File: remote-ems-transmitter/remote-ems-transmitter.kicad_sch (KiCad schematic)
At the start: 50 parts, among them IC1 Wio-E5, J1 Conn_01x04_Pin, J2 Conn_01x02, J3 Conn_01x02, J4 Conn_Coaxial, J5 USB_C_Receptacle_USB2.0, Q1 BSS138, SW1 SW_Push, SW2 SW_Push, SW3 SW_Push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

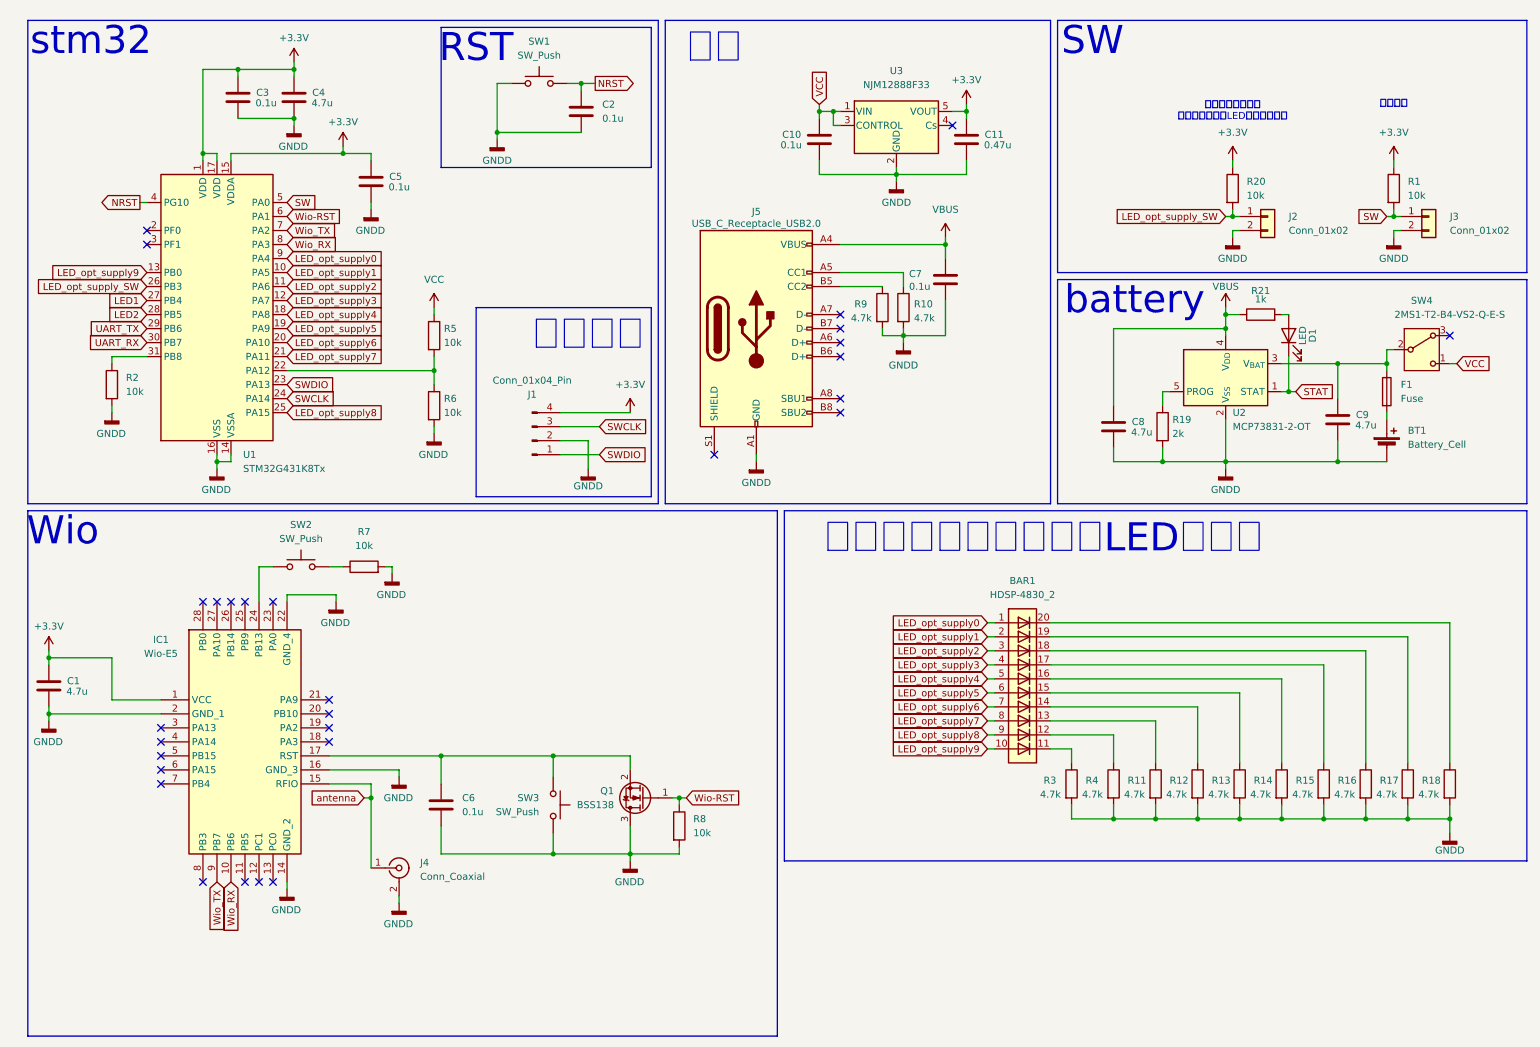
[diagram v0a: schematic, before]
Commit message: remote-ems-transmitter　ビア、シルク、LED以外完成
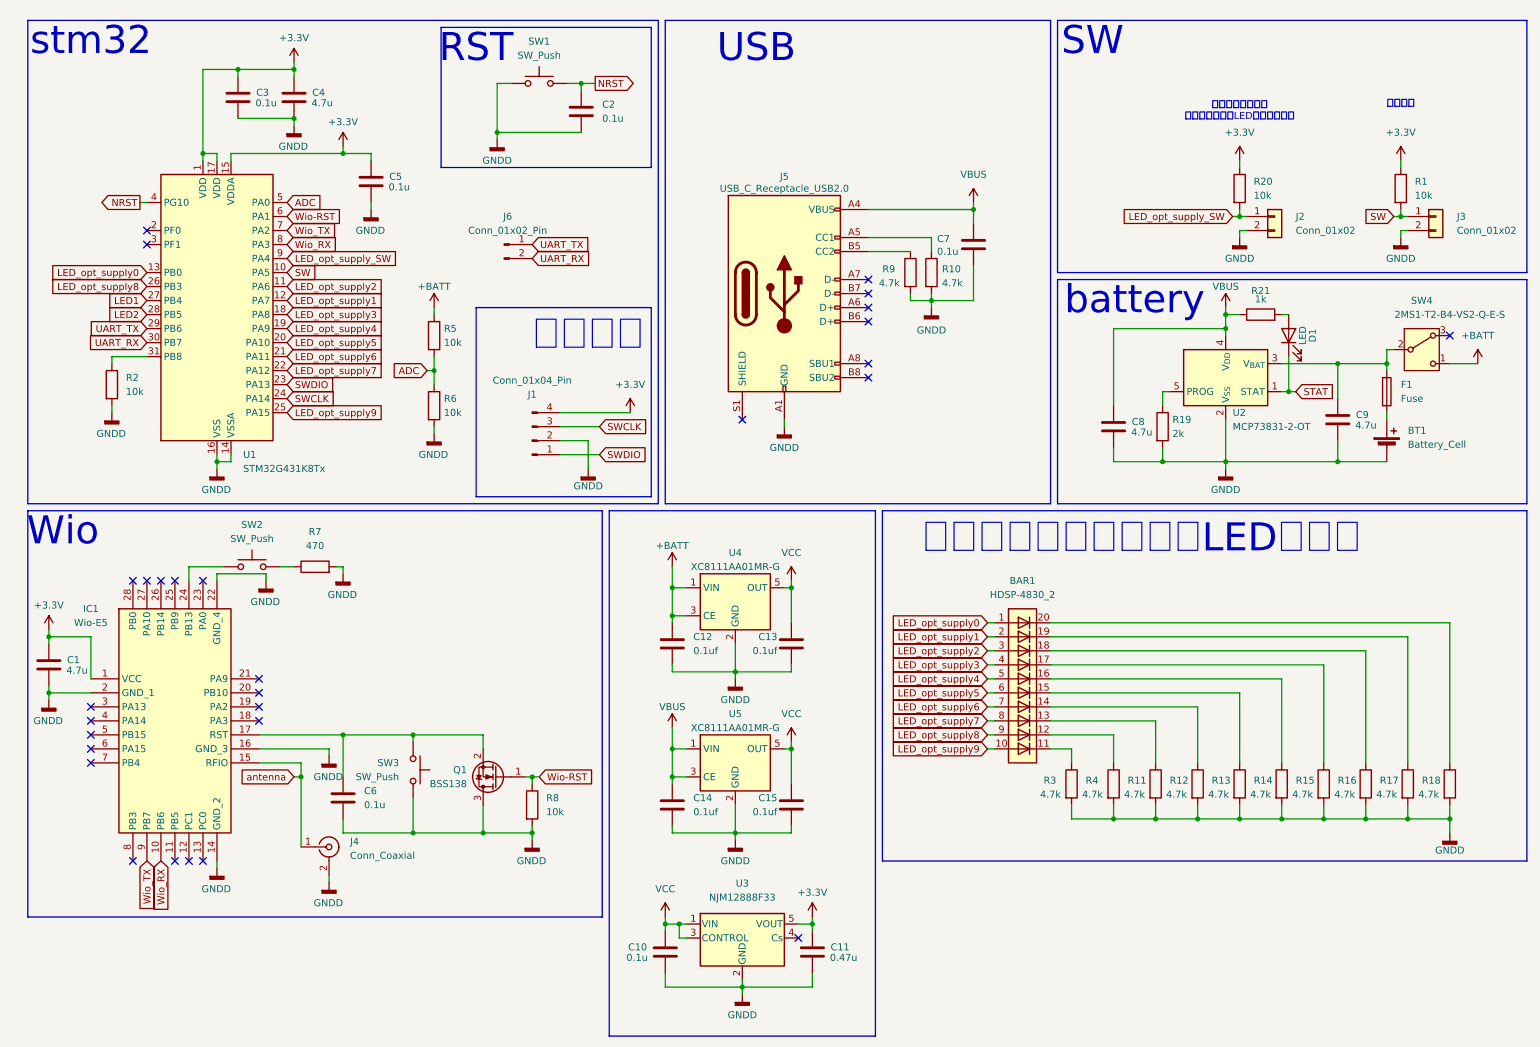
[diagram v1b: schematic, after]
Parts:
- added C12, C13, C14, C15: 0.1uf, Capacitor_SMD:C_0603_1608Metric_Pad1.08x0.95mm_HandSolder, symbol Device:C
- added J6: Conn_01x02_Pin, Connector_PinHeader_2.54mm:PinHeader_1x02_P2.54mm_Vertical, symbol Connector:Conn_01x02_Pin
- added U4, U5: XC8111AA01MR-G, Package_TO_SOT_SMD:SOT-23-5_HandSoldering, symbol Analog_Switch:MAX40200AUK
- BT1: footprint Connector_JST:JST_XH_B2B-XH-A_1x02_P2.50mm_Vertical -> Connector_JST:JST_PH_B2B-PH-K_1x02_P2.00mm_Vertical
- R7: value 10k -> 470
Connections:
- net GNDD: now also C12.2, C13.2, C14.2, C15.2, U4.2 (GND), U5.2 (GND)
- net LED_opt_supply0: now also U1.13 (PB0); no longer U1.9 (PA4)
- net LED_opt_supply1: now also U1.12 (PA7); no longer U1.10 (PA5)
- net LED_opt_supply3: now also U1.18 (PA8); no longer U1.12 (PA7)
- net LED_opt_supply4: now also U1.19 (PA9); no longer U1.18 (PA8)
- net LED_opt_supply5: now also U1.20 (PA10); no longer U1.19 (PA9)
- net LED_opt_supply6: now also U1.21 (PA11); no longer U1.20 (PA10)
- net LED_opt_supply7: now also U1.22 (PA12); no longer U1.21 (PA11)
- net LED_opt_supply8: now also U1.26 (PB3); no longer U1.25 (PA15)
- net LED_opt_supply9: now also U1.25 (PA15); no longer U1.13 (PB0)
- net LED_opt_supply_SW: now also U1.9 (PA4); no longer U1.26 (PB3)
- net SW: now also U1.10 (PA5); no longer U1.5 (PA0)
- net UART_RX: now also J6.2 (Pin_2)
- net UART_TX: now also J6.1 (Pin_1)
- net VBUS: now also C14.1, U5.1 (VIN), U5.3 (CE)
- net VCC: now also C13.1, C15.1, U4.5 (OUT), U5.5 (OUT); no longer R5.1, SW4.1 (C)
- net ADC: now reaches R5.2, R6.1
- net ADC: now also U1.5 (PA0); no longer U1.22 (PA12)
- new net +BATT: C12.1, R5.1, SW4.1 (C), U4.1 (VIN), U4.3 (CE)
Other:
- note added: "USB"
- note removed: "電源"
- moved on the sheet: C1, C10, C11, C6, C7, IC1, J2, J3, J4, J5, Q1, R1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

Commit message: LED周り修正
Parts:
- removed R21: 1k, Resistor_SMD:R_0603_1608Metric_Pad0.98x0.95mm_HandSolder, symbol Device:R
- added BAR2: OSX40601-AO, 0Ikedalibrary:OSX40601-AO, symbol LED:HDSP-4830_2
- added D2: LED, LED_THT:LED_D5.0mm_FlatTop, symbol Device:LED
- BAR1: value HDSP-4830_2 -> OSX05201-GGR1; footprint Display:HDSP-4830 -> 0Ikedalibrary:OSX05201-GGR1
- D1: footprint LED_SMD:LED_0603_1608Metric_Pad1.05x0.95mm_HandSolder -> LED_THT:LED_D5.0mm_FlatTop
- R3: value 4.7k -> 100
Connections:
- net +3.3V: now also BAR2.1 (A), BAR2.3 (A), BAR2.5 (A), BAR2.7 (K)
- net GNDD: now also D2.1 (K); no longer R11.2, R12.2, R13.2, R3.2, R4.2
- net LED1: now also D2.2 (A)
- net SW: now also R11.2, R12.2, R13.2, R4.2
- net VBUS: now also D1.2 (A)
- net Wio-RST: now also R3.1; no longer Q1.1 (G), R8.1
- net at R14.1: now also BAR1.6 (K); no longer BAR1.16 (K)
- net at R18.1: now also BAR1.10 (K); no longer BAR1.20 (K)
- net at R4.1: now also BAR2.8 (K); no longer BAR1.12 (K)
- net at R11.1: now also BAR2.6 (K); no longer BAR1.13 (K)
- net at R12.1: now also BAR2.4 (A); no longer BAR1.14 (K)
- net at R13.1: now also BAR2.2 (A); no longer BAR1.15 (K)
- net at R15.1: now also BAR1.7 (K); no longer BAR1.17 (K)
- net at R16.1: now also BAR1.8 (K); no longer BAR1.18 (K)
- net at R17.1: now also BAR1.9 (K); no longer BAR1.19 (K)
- net LED2: no longer names the net of U1.28 (PB5)
- net LED_opt_supply5: no longer names the net of U1.20 (PA10)
- net LED_opt_supply5: no longer BAR1.6 (A)
- net LED_opt_supply6: no longer names the net of U1.21 (PA11)
- net LED_opt_supply6: no longer BAR1.7 (A)
- net LED_opt_supply7: no longer names the net of U1.22 (PA12)
- net LED_opt_supply7: no longer BAR1.8 (A)
- net LED_opt_supply8: no longer names the net of U1.26 (PB3)
- net LED_opt_supply8: no longer BAR1.9 (A)
- net LED_opt_supply9: no longer names the net of U1.25 (PA15)
- net LED_opt_supply9: no longer BAR1.10 (A)
- new net: Q1.1 (G), R3.2, R8.1
- no-connect marks 29 -> 35
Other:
- note added: "LED"
- note removed: "バッテリー残量監視用LEDアレイ"
- moved on the sheet: R11, R12, R13, R4

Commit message: LED仕様変更
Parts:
- added Q2: BSS138, Package_TO_SOT_SMD:SOT-23, symbol Transistor_FET:BSS138
- added R21: 100, Resistor_SMD:R_0603_1608Metric_Pad0.98x0.95mm_HandSolder, symbol Device:R
- added R22: 10k, Resistor_SMD:R_0603_1608Metric_Pad0.98x0.95mm_HandSolder, symbol Device:R
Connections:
- net +3.3V: now also BAR2.4 (A), BAR2.8 (K); no longer BAR2.3 (A), BAR2.7 (K)
- net GNDD: now also Q2.3 (D), R22.2
- net SW: no longer R11.2, R12.2, R13.2, R4.2
- net at R4.1: now also BAR2.7 (K); no longer BAR2.8 (K)
- net at R12.1: now also BAR2.3 (A); no longer BAR2.4 (A)
- net emergency_stop_LED: now reaches U1.20 (PA10)
- net emergency_stop_LED: now also R21.1
- new net: Q2.1 (G), R21.2, R22.1
- new net: Q2.2 (S), R11.2, R12.2, R13.2, R4.2
- no-connect marks 35 -> 34
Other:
- moved on the sheet: D2

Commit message: ビア打ち、シルク修正中　残りは別日に対応します
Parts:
- added D3: LED, LED_SMD:LED_0603_1608Metric_Pad1.05x0.95mm_HandSolder, symbol Device:LED
- added R23: 1k, Resistor_SMD:R_0603_1608Metric_Pad0.98x0.95mm_HandSolder, symbol Device:R
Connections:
- net GNDD: now also D3.1 (K)
- net VBUS: now also R23.1
- new net: D3.2 (A), R23.2
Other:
- moved on the sheet: D2, R21, R22

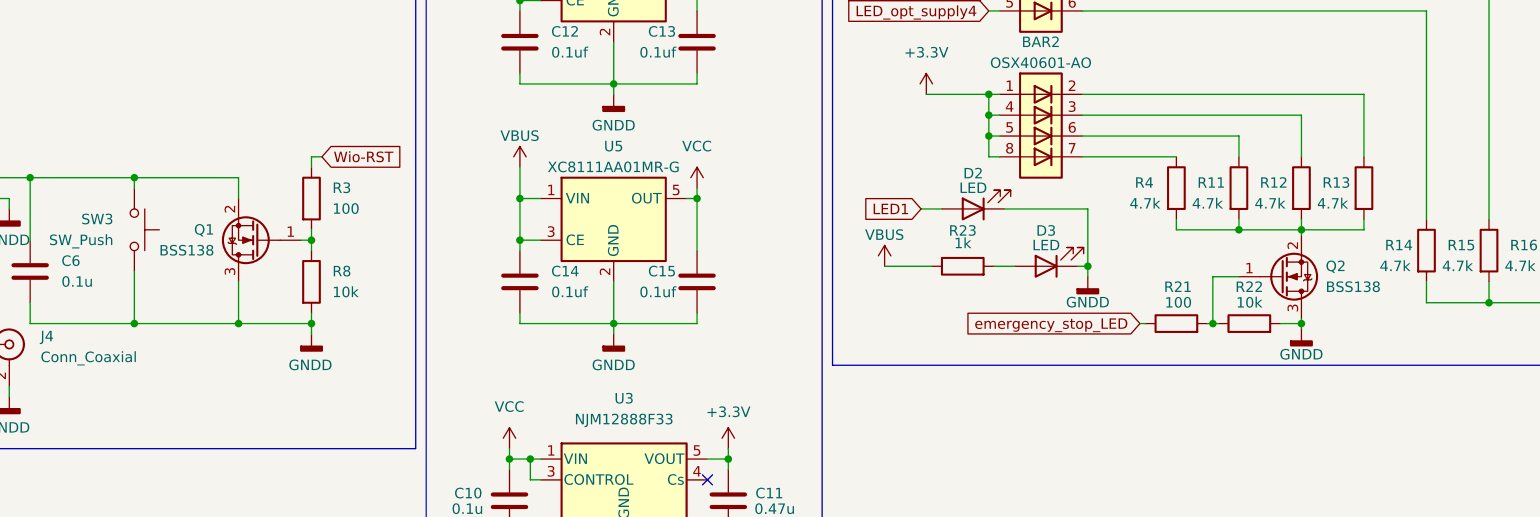
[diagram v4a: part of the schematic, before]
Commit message: FETの向きを修正 ガーバー出力
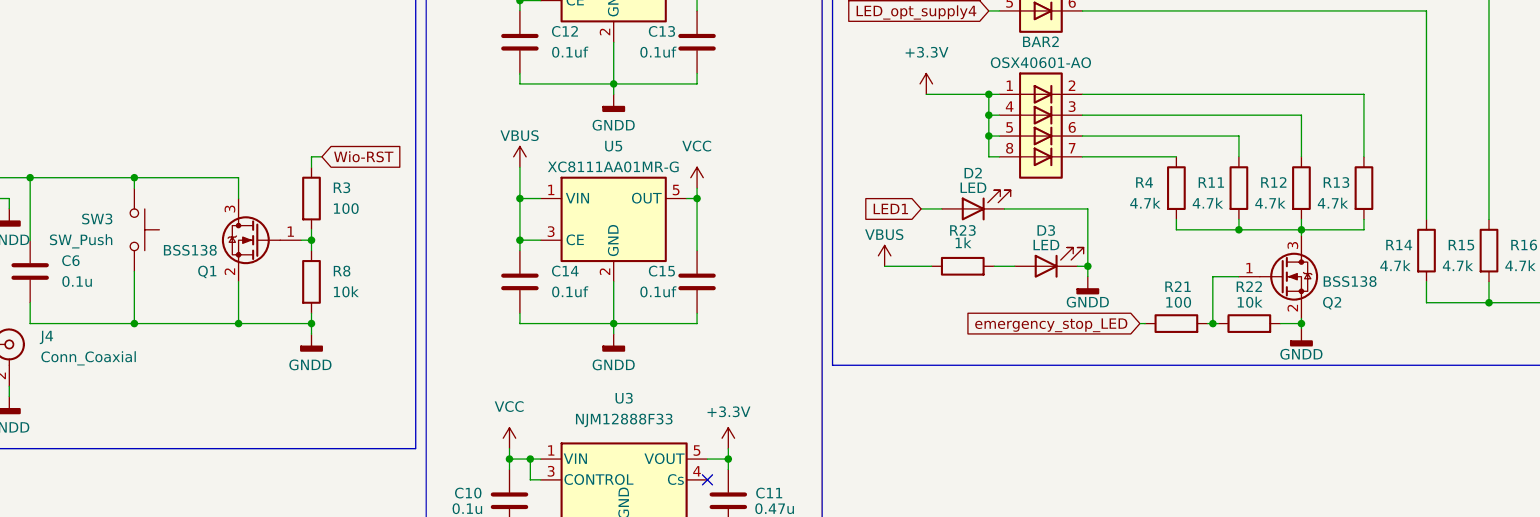
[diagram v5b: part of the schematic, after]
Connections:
- net GNDD: now also Q1.2 (S), Q2.2 (S); no longer Q1.3 (D), Q2.3 (D)
- net at R11.2, R12.2, R13.2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: now also Q2.3 (D); no longer Q2.2 (S)
- net at C6.1, IC1.17 (RST), SW3.2: now also Q1.3 (D); no longer Q1.2 (S)
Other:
- moved on the sheet: Q1
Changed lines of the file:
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@@
 		(lib_id "Transistor_FET:BSS138")
 		(at 222.25 154.305 0)
-		(mirror x)
 		(unit 1)
 		(exclude_from_sim no)
@@
 		(dnp no)
 		(property "Reference" "Q2"
-			(at 227.7364 153.0349 0)
+			(at 227.33 157.48 0)
 			(effects
 				(font
@@
 		)
 		(property "Value" "BSS138"
-			(at 227.7364 155.5749 0)
+			(at 227.33 154.94 0)
 			(effects
 				(font
@@
 		)
 		(property "Footprint" "Package_TO_SOT_SMD:SOT-23"
-			(at 227.33 152.4 0)
+			(at 227.33 156.21 0)
 			(effects
 				(font
@@
 	(symbol
 		(lib_id "Transistor_FET:BSS138")
-		(at 97.79 149.86 180)
+		(at 97.79 149.86 0)
+		(mirror y)
 		(unit 1)
 		(exclude_from_sim no)
@@
 		(dnp no)
 		(property "Reference" "Q1"
-			(at 92.3036 148.5899 0)
+			(at 92.71 153.67 0)
 			(effects
 				(font
@@
 		)
 		(property "Value" "BSS138"
-			(at 92.3036 151.1299 0)
+			(at 92.71 151.13 0)
 			(effects
 				(font
@@
 		)
 		(property "Footprint" "Package_TO_SOT_SMD:SOT-23"
-			(at 92.71 147.955 0)
-			(effects
-				(font
+			(at 92.71 151.765 0)
+			(effects
+				(font
